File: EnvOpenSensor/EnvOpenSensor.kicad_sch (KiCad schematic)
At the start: 76 parts, among them IC1 IS31FL3730-QFLS2-TR, IC2 IS31FL3730-QFLS2-TR, IC3 IS31FL3730-QFLS2-TR, IC4 IS31FL3730-QFLS2-TR, J1 HRO_TYPE-C-31-M-12, J2 AVR-ISP-6, SW1 SW_Push, SW2 SW_Push, SW3 SW_Push, SW4 SW_Push, U0 TCA9548ARGER, U1 SCD41-D-R2, U2 Si7021-A20, U4 ATtiny85-20S, U5 TPS63001DRCR

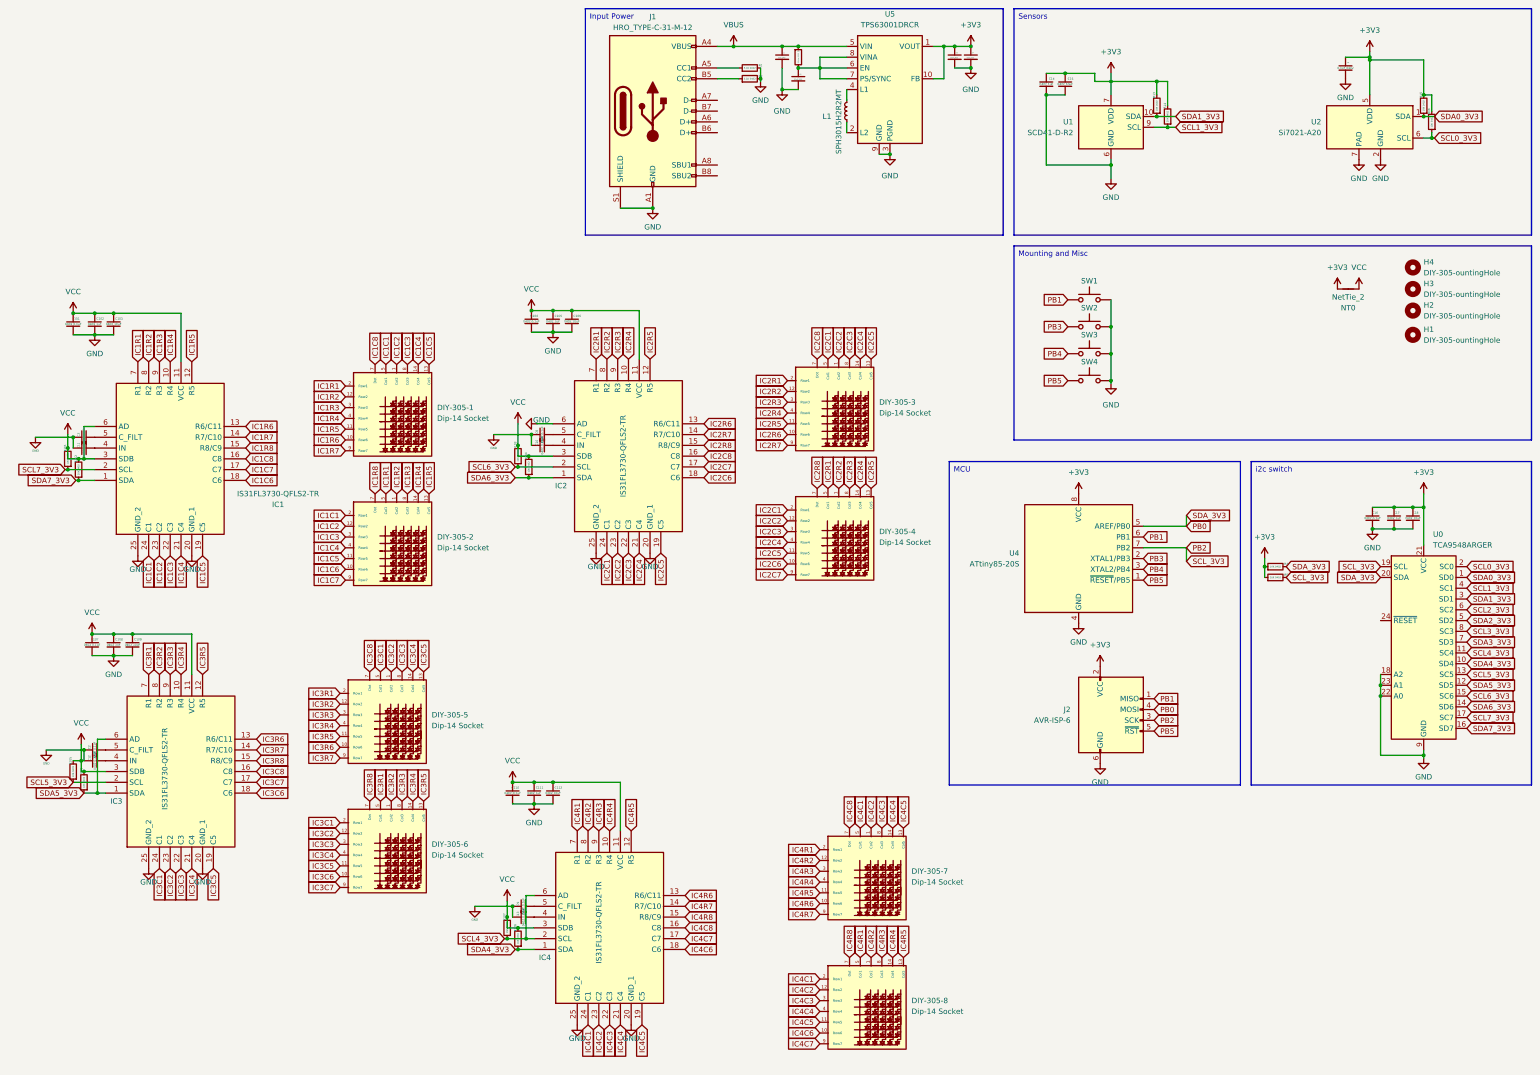
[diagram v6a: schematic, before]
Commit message: recognised issues with the design, redid schematic to include onboard LEDs and a RP2040, started re-work on PCB
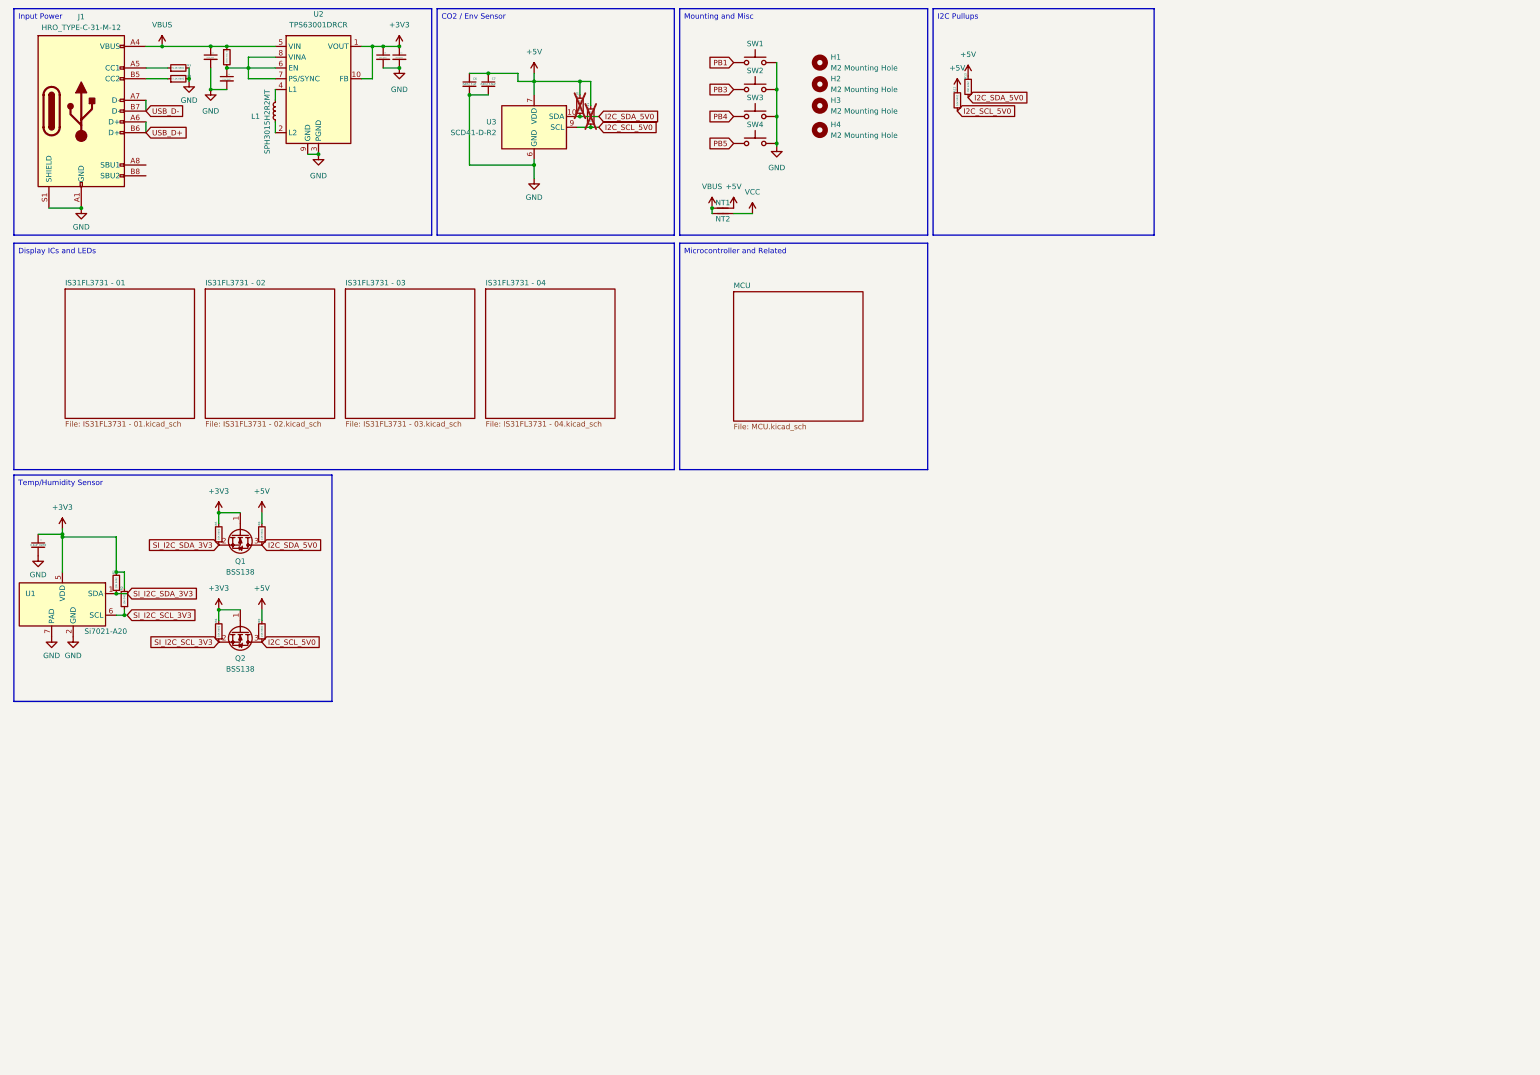
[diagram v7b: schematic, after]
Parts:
- removed C10, C11, C12, C13: 0402 0.22uF, Capacitor_SMD:C_0402_1005Metric, symbol Device:C_Small
- removed C101, C104, C107, C110, C16, C2, C3, C8, C9: 0402 0.1uF, Capacitor_SMD:C_0402_1005Metric, symbol Device:C_Small
- removed C102, C105, C108, C111, C17: 0402 1uF, Capacitor_SMD:C_0402_1005Metric, symbol Device:C_Small
- removed C103, C106, C109, C112, C18: 0402 10uF, Capacitor_SMD:C_0402_1005Metric, symbol Device:C_Small
- removed DIY-305-1, DIY-305-2, DIY-305-3, DIY-305-4, DIY-305-5, DIY-305-6, DIY-305-7, DIY-305-8: Dip-14 Socket, Package_DIP:DIP-14_W7.62mm_Socket, symbol ltp-305g:LTP-305G
- removed IC1, IC2, IC3, IC4: IS31FL3730-QFLS2-TR, Package_DFN_QFN:QFN-24-1EP_4x4mm_P0.5mm_EP2.6x2.6mm_ThermalVias, symbol IS31FL3730-QFLS2-TR:IS31FL3730-QFLS2-TR
- removed J2: AVR-ISP-6, Connector_PinHeader_2.54mm:PinHeader_2x03_P2.54mm_Vertical, symbol Connector:AVR-ISP-6
- removed NT0: NetTie_2, NetTie:NetTie-2_SMD_Pad0.5mm, symbol Device:NetTie_2
- removed R101, R102, R103, R104, R105, R106, R107, R108, R4: 10K 0402, Resistor_SMD:R_0402_1005Metric, symbol Device:R_Small
- removed U0: TCA9548ARGER, Package_DFN_QFN:Texas_RGE0024C_EP2.1x2.1mm, symbol Interface_Expansion:TCA9548ARGER
- removed U4: ATtiny85-20S, Package_SO:SOIC-8W_5.3x5.3mm_P1.27mm, symbol MCU_Microchip_ATtiny:ATtiny85-20S
- added NT1, NT2: NetTie_2, NetTie:NetTie-2_THT_Pad1.0mm, symbol Device:NetTie_2
- added Q1, Q2: BSS138, Package_TO_SOT_SMD:SOT-23, symbol Transistor_FET:BSS138
- added R12, R13, R6, R8, R9: 10K 0402, Resistor_SMD:R_0402_1005Metric, symbol Device:R_Small
- H1: renamed from H4; value DIY-305-ountingHole -> M2 Mounting Hole
- H2: renamed from H3; value DIY-305-ountingHole -> M2 Mounting Hole
- H3: renamed from H2; value DIY-305-ountingHole -> M2 Mounting Hole
- H4: renamed from H1; value DIY-305-ountingHole -> M2 Mounting Hole
- R10: renamed from R13; now not fitted
- R11: renamed from R14; now not fitted
- renumbered C4 to C1, C1 to C2, C5 to C3, C6 to C4, C7 to C5, C14 to C6, C15 to C7, R15 to R1, R16 to R2, R1 to R3, R2 to R4, R6 to R7, U2 to U1, U5 to U2, U1 to U3
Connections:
- net PB2 is gone; now on net +3V3: R5.2
- net +3V3: now also Q1.1 (G), Q2.1 (G), R6.2; no longer C6.1, C7.1, R10.2, R11.2, R5.1, U3.19 (VDD), U3.7 (VDD)
- net VBUS: now also NT1.1, NT2.1
- net VCC: now also NT2.2
- net USB_D+: now reaches J1.A6 (D+)
- net USB_D+: now also J1.B6 (D+)
- net USB_D-: now reaches J1.A7 (D-)
- net USB_D-: now also J1.B7 (D-)
- net SCL0_3V3 renamed SI_I2C_SCL_3V3
- net SI_I2C_SCL_3V3: now also Q2.2 (S), R6.1
- net SCL1_3V3 renamed I2C_SCL_5V0
- net I2C_SCL_5V0: now also Q2.3 (D), R12.1, R9.1
- net SDA0_3V3 renamed SI_I2C_SDA_3V3
- net SI_I2C_SDA_3V3: now also R5.1, Q1.2 (S)
- net SDA1_3V3 renamed I2C_SDA_5V0
- net I2C_SDA_5V0: now also Q1.3 (D), R13.1, R8.1
- new net +5V: C6.1, C7.1, NT1.2, R10.2, R11.2, R12.2, R13.2, R8.2, R9.2, U3.19 (VDD), U3.7 (VDD)
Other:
- added sheet IS31FL3731 - 01 (IS31FL3731 - 01.kicad_sch)
- added sheet IS31FL3731 - 02 (IS31FL3731 - 02.kicad_sch)
- added sheet IS31FL3731 - 03 (IS31FL3731 - 03.kicad_sch)
- added sheet IS31FL3731 - 04 (IS31FL3731 - 04.kicad_sch)
- added sheet MCU (MCU.kicad_sch)
- moved on the sheet: C1, C2, C3, C4, C5, C6, C7, H1, H2, H3, H4, J1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

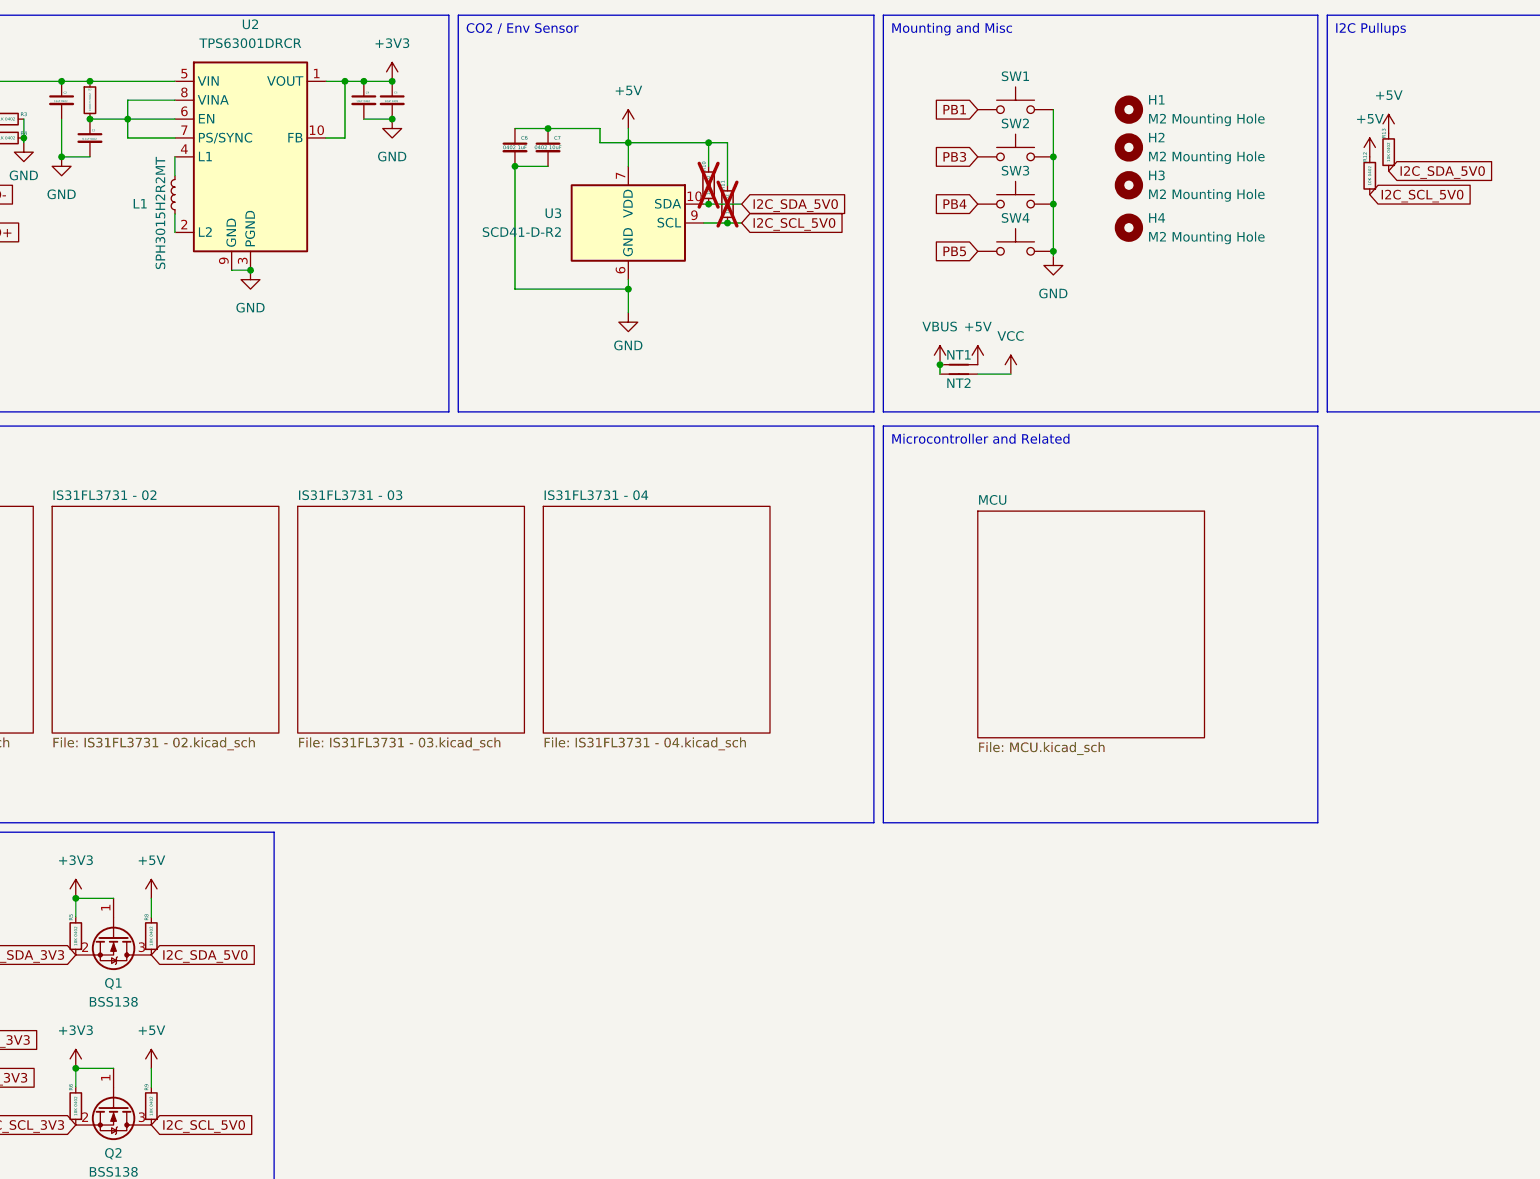
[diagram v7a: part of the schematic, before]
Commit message: finished routing up board, needs a double-check
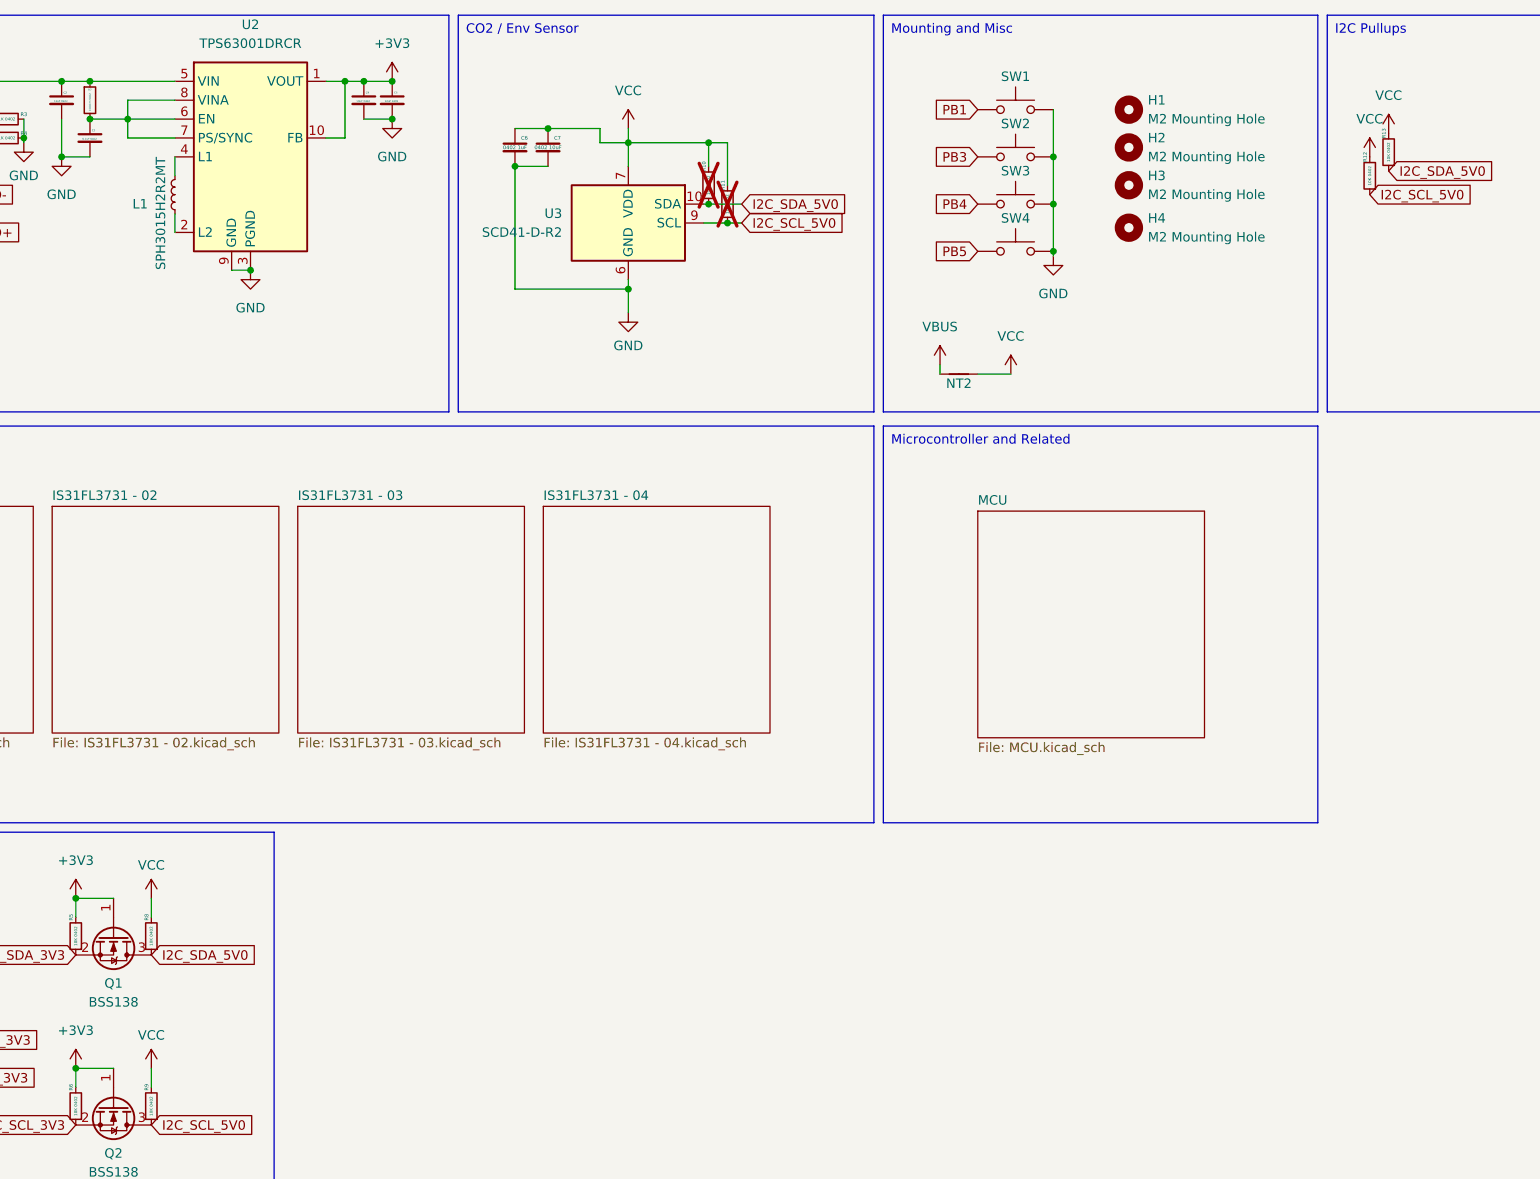
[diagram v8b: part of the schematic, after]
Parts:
- removed NT1: NetTie_2, NetTie:NetTie-2_THT_Pad1.0mm, symbol Device:NetTie_2
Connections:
- net +5V is gone; now on net VCC: C6.1, C7.1, R10.2, R11.2, R12.2, R13.2, R8.2, R9.2, U3.19 (VDD), U3.7 (VDD)
